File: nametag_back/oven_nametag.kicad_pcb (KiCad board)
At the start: 2 copper layers, 100 x 75 mm, 92 parts, among them Q1 BSS138, Q10 BSS138, Q11 BSS138, Q12 BSS138, Q13 BSS138, Q14 BSS138, Q15 BSS138, Q16 BSS138, Q17 BSS138, Q18 BSS138, Q19 BSS138, Q2 BSS138, Q20 BSS138, Q21 BSS138, Q22 BSS138, Q23 BSS138, Q24 BSS138, Q25 BSS138, Q26 BSS138, Q27 BSS138, Q3 BSS138, Q4 BSS138, Q5 BSS138, Q6 BSS138, Q7 BSS138, Q8 BSS138, Q9 BSS138, SW2 SW_SPDT, U1 TPS613221ADBV

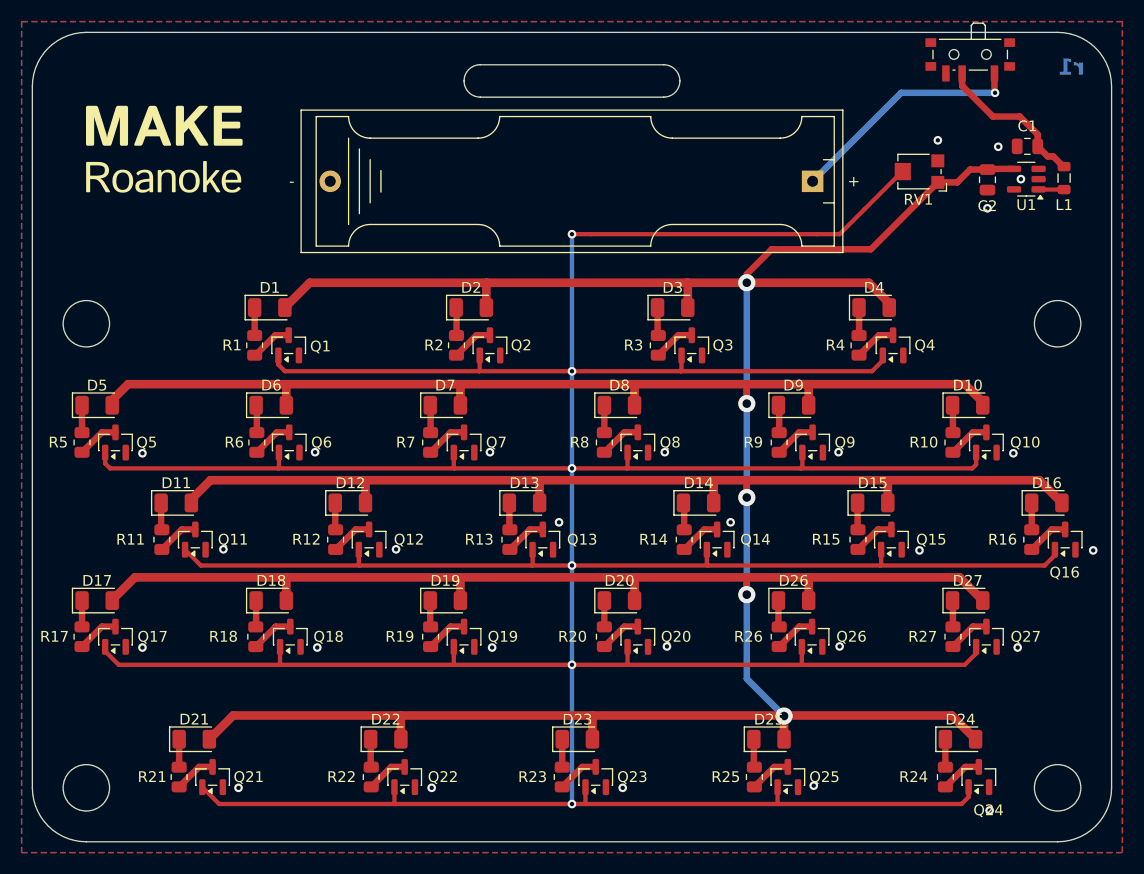
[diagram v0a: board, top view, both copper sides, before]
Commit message: Remove all but one low-side mosfets
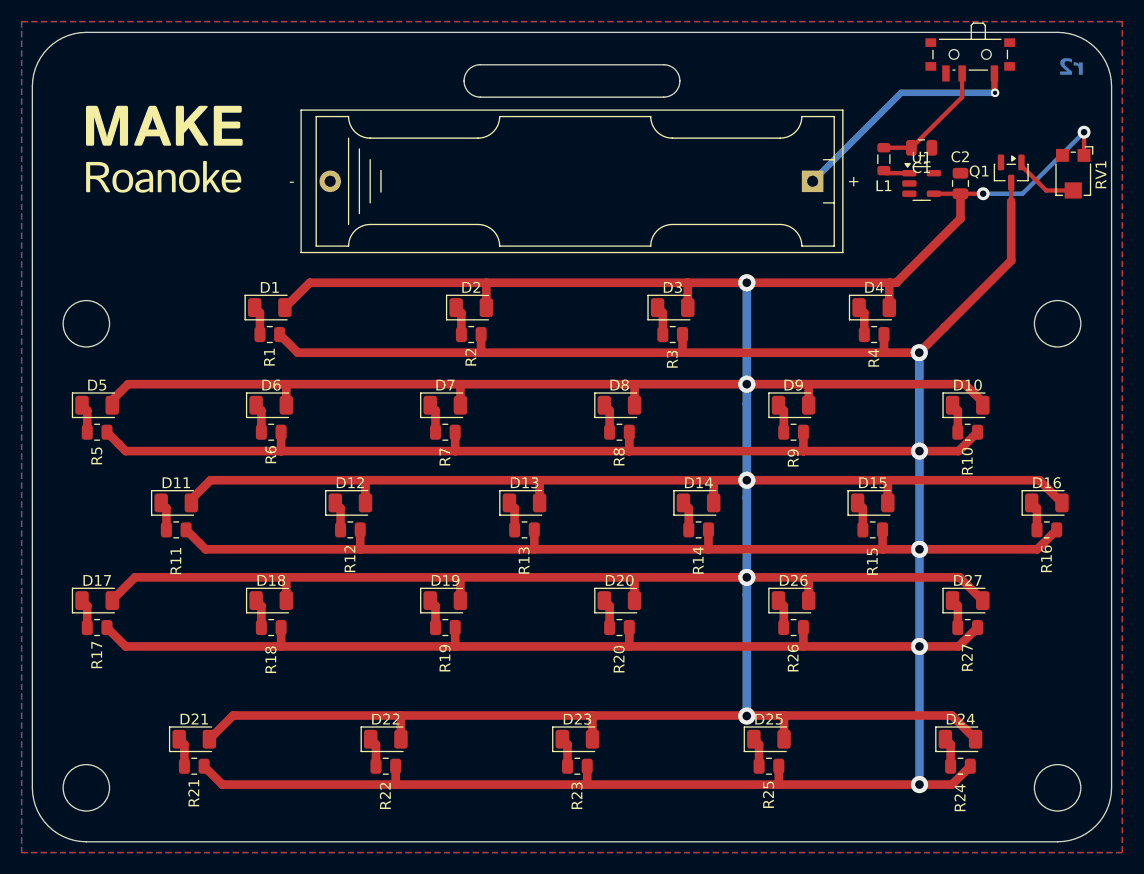
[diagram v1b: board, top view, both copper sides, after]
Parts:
- removed Q10, Q11, Q12, Q13, Q14, Q15, Q16, Q17, Q18, Q19, Q2, Q20, Q21, Q22, Q23, Q24, Q25, Q26, Q27, Q3, Q4, Q5, Q6, Q7, Q8, Q9: BSS138, Package_TO_SOT_SMD:SOT-23
- moved Q1 68.8 mm to (242.7, 63.0), turned to -90 degrees
- moved L1 16.8 mm to (230.9, 61.8)
- moved RV1 14.4 mm to (248.4, 63.2), turned to -90 degrees
- moved C1 9.80 mm to (234.4, 60.7), turned to 0 degrees
- moved U1 9.71 mm to (234.4, 64.0), turned to 0 degrees
- moved C2 2.52 mm to (238.0, 64.0), turned to 90 degrees
- moved R1 1.72 mm to (174.0, 78.0), turned to 0 degrees
- moved R21 1.72 mm to (167.0, 118.0), turned to 0 degrees
- moved R23 1.72 mm to (202.5, 118.0), turned to 0 degrees
- moved R24 1.72 mm to (238.0, 118.0), turned to 0 degrees
- moved R4 1.72 mm to (230.0, 78.0), turned to 0 degrees
- moved R2 1.69 mm to (192.7, 78.0), turned to 0 degrees
- moved R5 1.69 mm to (158.0, 87.0), turned to 0 degrees
- moved R8 1.69 mm to (206.4, 87.0), turned to 0 degrees
- moved R22 1.68 mm to (184.8, 118.0), turned to 0 degrees
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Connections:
- Q1 pad 3: Net-(Q1-D) -> /LEDs/LIGHT_CTRL
- R1 pad 2: Net-(Q1-D) -> /LEDs/LIGHT_CTRL
- R10 pad 2: Net-(Q10-D) -> /LEDs/LIGHT_CTRL
- R11 pad 2: Net-(Q11-D) -> /LEDs/LIGHT_CTRL
- R12 pad 2: Net-(Q12-D) -> /LEDs/LIGHT_CTRL
- R13 pad 2: Net-(Q13-D) -> /LEDs/LIGHT_CTRL
- R14 pad 2: Net-(Q14-D) -> /LEDs/LIGHT_CTRL
- R15 pad 2: Net-(Q15-D) -> /LEDs/LIGHT_CTRL
- R16 pad 2: Net-(Q16-D) -> /LEDs/LIGHT_CTRL
- R17 pad 2: Net-(Q17-D) -> /LEDs/LIGHT_CTRL
- R18 pad 2: Net-(Q18-D) -> /LEDs/LIGHT_CTRL
- R19 pad 2: Net-(Q19-D) -> /LEDs/LIGHT_CTRL
- R2 pad 2: Net-(Q2-D) -> /LEDs/LIGHT_CTRL
- R20 pad 2: Net-(Q20-D) -> /LEDs/LIGHT_CTRL
- R21 pad 2: Net-(Q21-D) -> /LEDs/LIGHT_CTRL
- R22 pad 2: Net-(Q22-D) -> /LEDs/LIGHT_CTRL
- R23 pad 2: Net-(Q23-D) -> /LEDs/LIGHT_CTRL
- R24 pad 2: Net-(Q24-D) -> /LEDs/LIGHT_CTRL
- R25 pad 2: Net-(Q25-D) -> /LEDs/LIGHT_CTRL
- R26 pad 2: Net-(Q26-D) -> /LEDs/LIGHT_CTRL
- R27 pad 2: Net-(Q27-D) -> /LEDs/LIGHT_CTRL
- R3 pad 2: Net-(Q3-D) -> /LEDs/LIGHT_CTRL
- R4 pad 2: Net-(Q4-D) -> /LEDs/LIGHT_CTRL
- R5 pad 2: Net-(Q5-D) -> /LEDs/LIGHT_CTRL
- R6 pad 2: Net-(Q6-D) -> /LEDs/LIGHT_CTRL
- R7 pad 2: Net-(Q7-D) -> /LEDs/LIGHT_CTRL
- R8 pad 2: Net-(Q8-D) -> /LEDs/LIGHT_CTRL
- R9 pad 2: Net-(Q9-D) -> /LEDs/LIGHT_CTRL
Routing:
- net /LEDs/CTRL: track 491.5 -> 6.05 mm, vias 6 -> 0
- net /LEDs/LIGHT_CTRL: track 0.00 -> 469.6 mm, vias 0 -> 5
- net +3V3: track 491.3 -> 486.3 mm, vias 5 -> 7
- net Net-(Q4-D): track 4.26 -> 0.00 mm
- net Net-(Q18-D): track 3.97 -> 0.00 mm
- net Net-(Q1-D): track 3.94 -> 0.00 mm
- net Net-(Q16-D): track 3.90 -> 0.00 mm
- net Net-(Q12-D): track 3.90 -> 0.00 mm
- net Net-(Q11-D): track 3.90 -> 0.00 mm
- net Net-(Q9-D): track 3.87 -> 0.00 mm
- net Net-(Q8-D): track 3.87 -> 0.00 mm
- net Net-(Q7-D): track 3.87 -> 0.00 mm
- net Net-(Q5-D): track 3.87 -> 0.00 mm
- net Net-(Q3-D): track 3.87 -> 0.00 mm
- net Net-(Q27-D): track 3.87 -> 0.00 mm
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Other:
- board text added: "r2"
- board text removed: "r1"

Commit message: Push new fab files
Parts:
- D1, D10, D11, D12, D13, D14, D15, D16, D17, D18, D19, D2, D20, D26, D27, D3, D4, D5, D6, D7, D8, D9: value LED -> YELLOW
- D21, D22, D23, D24, D25: value LED -> GREEN
- H1, H2, H3, H4: footprint MountingHole:MountingHole_4.3mm_M4 -> MountingHole:MountingHole_3.2mm_M3
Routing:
- net GND: vias 0 -> 36
